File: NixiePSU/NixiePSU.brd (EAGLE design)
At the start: 55.5 x 35.5 mm, 18 parts, among them IC1 NE555, Q1 BUZ11BV, T1 BC547

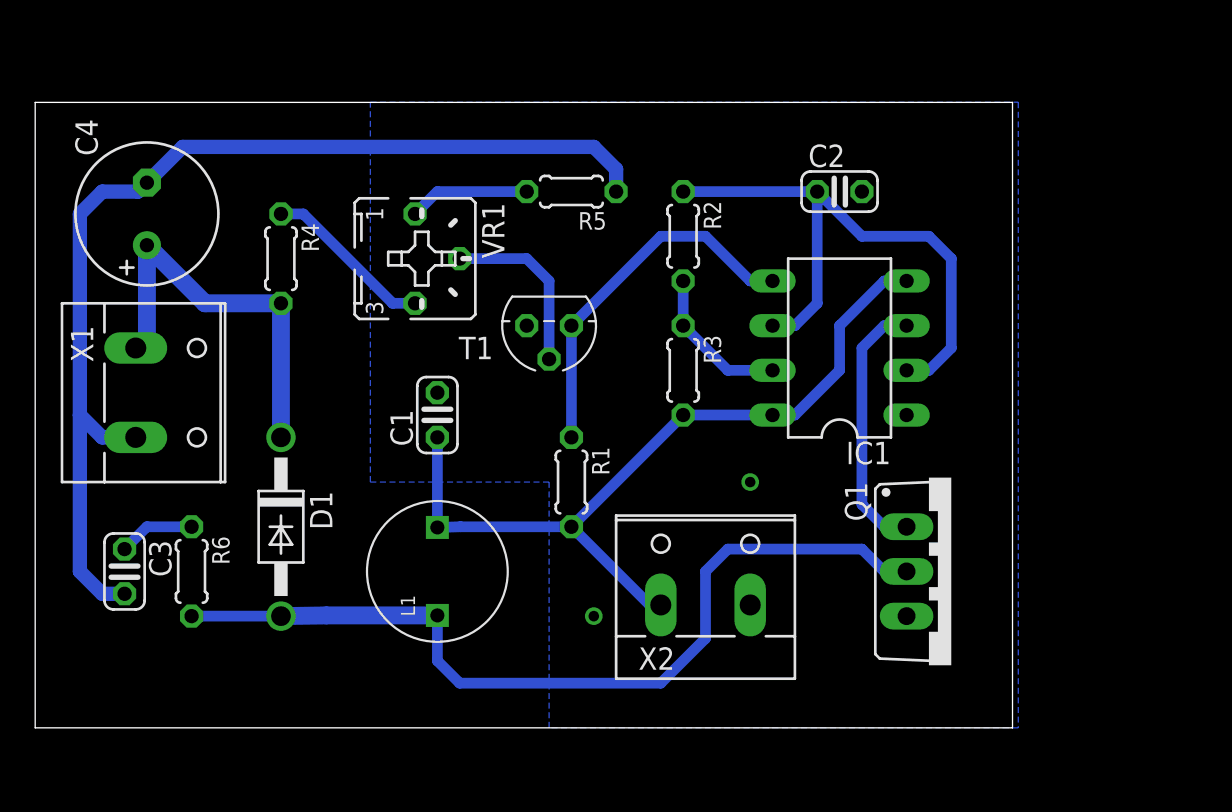
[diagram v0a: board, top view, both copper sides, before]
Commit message: Swap some components.
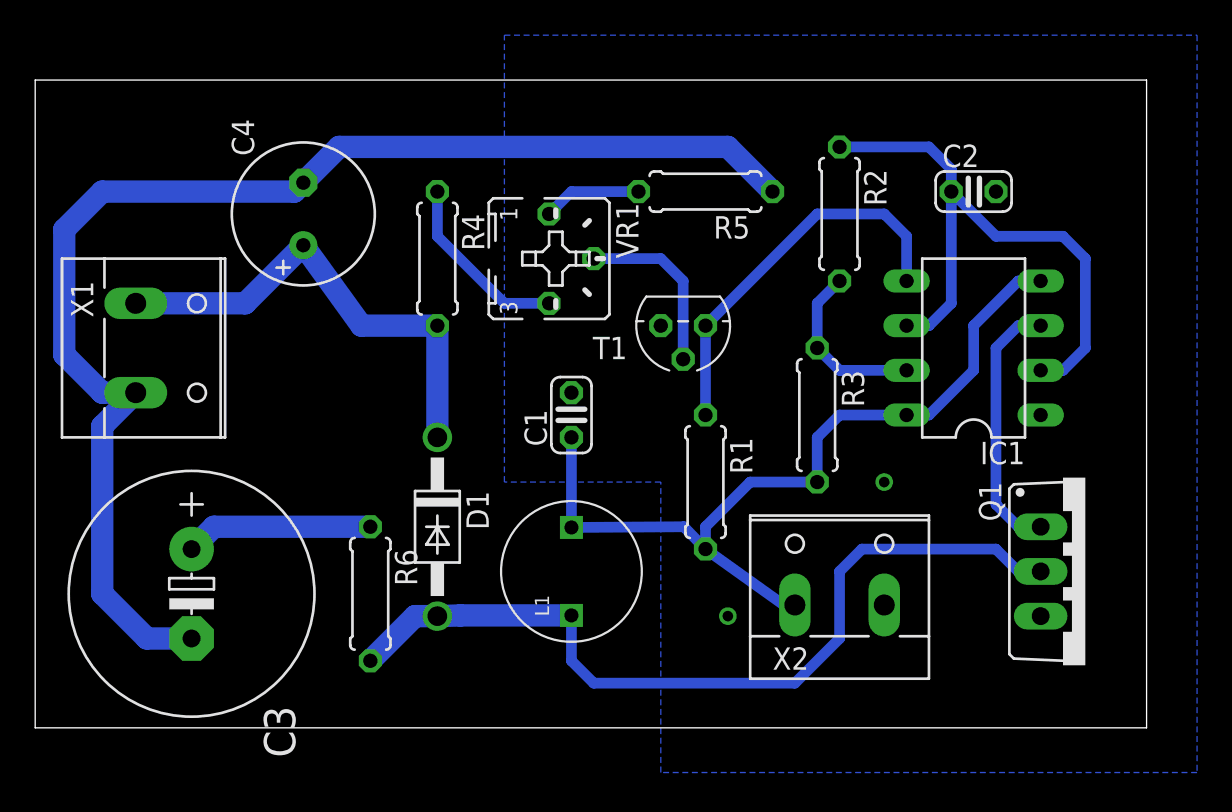
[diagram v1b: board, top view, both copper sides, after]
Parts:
- C3: device rcl:C025-024X044 -> rcl:E5-13
- R1, R2, R3, R4, R5, R6: device rcl:0204/5 -> rcl:0207/7
- moved R6 10.2 mm to (19.1, 7.62)
- moved R2 8.98 mm to (45.7, 29.2)
- moved C4 8.89 mm to (15.2, 29.2)
- moved D1 8.89 mm to (22.9, 11.4)
- moved R4 8.89 mm to (22.9, 26.7)
- moved R3 8.03 mm to (44.5, 17.8)
- moved C2 7.62 mm to (53.3, 30.5)
- moved IC1 7.62 mm to (53.3, 21.6)
- moved C1 7.62 mm to (30.5, 17.8)
- moved L1 7.62 mm to (30.5, 8.89)
- moved R1 7.62 mm to (38.1, 14.0)
- moved R5 7.62 mm to (38.1, 30.5)
- moved VR1 7.62 mm to (29.2, 26.7)
- moved Q1 7.62 mm to (59.7, 8.89)
- moved T1 7.62 mm to (36.8, 22.9)
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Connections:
- net GND: now also C3.-; no longer C3.2
- net N$9: now also C3.+; no longer C3.1
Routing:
- net GND: track 60.9 -> 73.7 mm
- net N$9: track 4.34 -> 10.7 mm
- net HV: track 22.7 -> 27.2 mm
- net VCC: track 46.0 -> 48.5 mm
- net N$2: track 49.7 -> 48.2 mm
- net N$7: track 6.88 -> 5.61 mm
- net N$5: track 20.9 -> 22.2 mm
- net N$3: track 8.67 -> 9.94 mm
- net N$4: track 9.72 -> 10.5 mm
- net N$10: track 34.4 -> 34.9 mm
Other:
- board size 55.5 x 35.5 mm -> 63.2 x 36.8 mm

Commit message: Rewire the threshold pin on the 555. Fix some ERC errors.
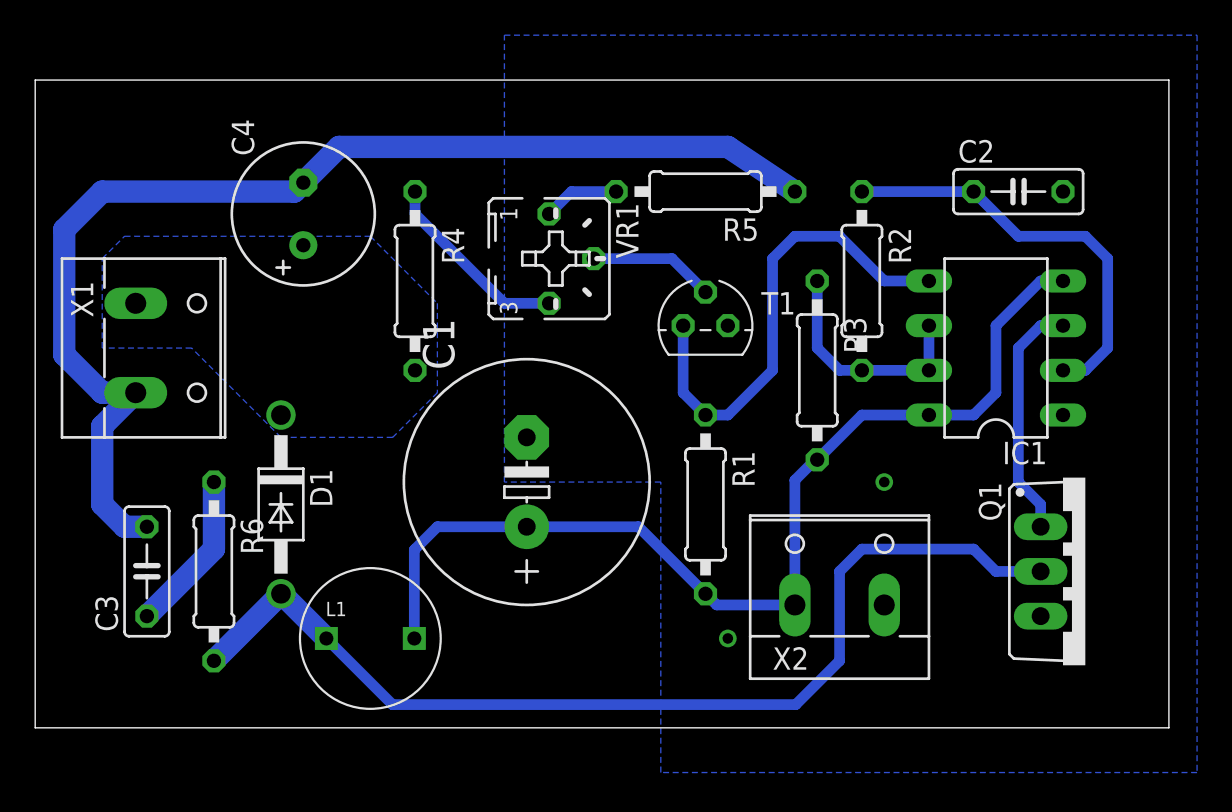
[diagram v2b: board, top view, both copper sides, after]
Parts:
- C1: device rcl:C025-024X044 -> rcl:E5-13
- C2: device rcl:C025-024X044 -> rcl:C050-025X075
- C3: device rcl:E5-13 -> rcl:C050-025X075
- R1, R2, R3, R4, R5, R6: device rcl:0207/7 -> rcl:0207/10
- moved L1 12.0 mm to (19.1, 5.08), turned to 0 degrees
- moved R6 8.98 mm to (10.2, 8.89)
- moved D1 8.98 mm to (14.0, 12.7)
- moved C1 4.58 mm to (27.9, 14.0)
- moved R2 4.02 mm to (47.0, 25.4)
- moved C3 2.84 mm to (6.35, 8.89), turned to 90 degrees
- moved C2 2.54 mm to (55.9, 30.5)
- moved R3 2.54 mm to (44.5, 20.3)
- moved R4 1.80 mm to (21.6, 25.4)
- moved T1 1.27 mm to (38.1, 22.9), turned to 0 degrees
- moved R1 1.27 mm to (38.1, 12.7)
- moved IC1 1.27 mm to (54.6, 21.6)
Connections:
- net GND: now also C1.-, C3.2; no longer C1.2, C3.-
- net N$10: no longer IC1.6
- net N$3: now also IC1.6
- net N$9: now also C3.1; no longer C3.+
- net VCC: now also C1.+; no longer C1.1
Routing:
- net HV: track 27.2 -> 0.00 mm
- net N$10: track 34.9 -> 23.7 mm
- net VCC: track 48.5 -> 59.0 mm
- net N$2: track 48.2 -> 58.3 mm
- net GND: track 73.7 -> 66.5 mm
- net N$6: track 22.2 -> 27.3 mm
- net N$3: track 9.94 -> 13.3 mm
- net N$8: track 10.1 -> 7.14 mm
- net N$9: track 10.7 -> 9.20 mm
- net N$1: track 15.0 -> 13.8 mm
- net N$7: track 5.61 -> 4.34 mm
- net N$4: track 10.5 -> 11.0 mm
- added copper zone on layer 16, net HV
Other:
- board size 63.2 x 36.8 mm -> 64.4 x 36.8 mm

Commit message: Bunch of random updated
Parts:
- R4: value 470 -> 470k
- R5: value 220k -> 1k2
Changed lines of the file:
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@@
 <?xml version="1.0" encoding="utf-8"?>
 <!DOCTYPE eagle SYSTEM "eagle.dtd">
-<eagle version="8.2.2">
+<eagle version="7.7.0">
 <drawing>
 <settings>
@@
 <grid distance="0.05" unitdist="inch" unit="inch" style="lines" multiple="1" display="no" altdistance="0.025" altunitdist="inch" altunit="inch"/>
 <layers>
-<layer number="1" name="Top" color="4" fill="1" visible="yes" active="yes"/>
-<layer number="16" name="Bottom" color="1" fill="1" visible="yes" active="yes"/>
-<layer number="17" name="Pads" color="2" fill="1" visible="yes" active="yes"/>
-<layer number="18" name="Vias" color="2" fill="1" visible="yes" active="yes"/>
-<layer number="19" name="Unrouted" color="6" fill="1" visible="yes" active="yes"/>
+<layer number="1" name="Top" color="4" fill="1" visible="no" active="yes"/>
+<layer number="16" name="Bottom" color="1" fill="1" visible="no" active="yes"/>
+<layer number="17" name="Pads" color="2" fill="1" visible="no" active="yes"/>
+<layer number="18" name="Vias" color="2" fill="1" visible="no" active="yes"/>
+<layer number="19" name="Unrouted" color="6" fill="1" visible="no" active="yes"/>
 <layer number="20" name="Dimension" color="15" fill="1" visible="yes" active="yes"/>
 <layer number="21" name="tPlace" color="7" fill="1" visible="yes" active="yes"/>
-<layer number="22" name="bPlace" color="7" fill="1" visible="yes" active="yes"/>
-<layer number="23" name="tOrigins" color="15" fill="1" visible="yes" active="yes"/>
-<layer number="24" name="bOrigins" color="15" fill="1" visible="yes" active="yes"/>
+<layer number="22" name="bPlace" color="7" fill="1" visible="no" active="yes"/>
+<layer number="23" name="tOrigins" color="15" fill="1" visible="no" active="yes"/>
+<layer number="24" name="bOrigins" color="15" fill="1" visible="no" active="yes"/>
 <layer number="25" name="tNames" color="7" fill="1" visible="yes" active="yes"/>
-<layer number="26" name="bNames" color="7" fill="1" visible="yes" active="yes"/>
+<layer number="26" name="bNames" color="7" fill="1" visible="no" active="yes"/>
 <layer number="27" name="tValues" color="7" fill="1" visible="yes" active="yes"/>
-<layer number="28" name="bValues" color="7" fill="1" visible="yes" active="yes"/>
-<layer number="29" name="tStop" color="7" fill="3" visible="yes" active="yes"/>
-<layer number="30" name="bStop" color="7" fill="6" visible="yes" active="yes"/>
-<layer number="31" name="tCream" color="7" fill="4" visible="yes" active="yes"/>
-<layer number="32" name="bCream" color="7" fill="5" visible="yes" active="yes"/>
-<layer number="33" name="tFinish" color="6" fill="3" visible="yes" active="yes"/>
-<layer number="34" name="bFinish" color="6" fill="6" visible="yes" active="yes"/>
-<layer number="35" name="tGlue" color="7" fill="4" visible="yes" active="yes"/>
-<layer number="36" name="bGlue" color="7" fill="5" visible="yes" active="yes"/>
-<layer number="37" name="tTest" color="7" fill="1" visible="yes" active="yes"/>
-<layer number="38" name="bTest" color="7" fill="1" visible="yes" active="yes"/>
-<layer number="39" name="tKeepout" color="4" fill="11" visible="yes" active="yes"/>
-<layer number="40" name="bKeepout" color="1" fill="11" visible="yes" active="yes"/>
-<layer number="41" name="tRestrict" color="4" fill="10" visible="yes" active="yes"/>
-<layer number="42" name="bRestrict" color="1" fill="10" visible="yes" active="yes"/>
-<layer number="43" name="vRestrict" color="2" fill="10" visible="yes" active="yes"/>
-<layer number="44" name="Drills" color="7" fill="1" visible="yes" active="yes"/>
-<layer number="45" name="Holes" color="7" fill="1" visible="yes" active="yes"/>
-<layer number="46" name="Milling" color="3" fill="1" visible="yes" active="yes"/>
-<layer number="47" name="Measures" color="7" fill="1" visible="yes" active="yes"/>
-<layer number="48" name="Document" color="7" fill="1" visible="yes" active="yes"/>
-<layer number="49" name="Reference" color="7" fill="1" visible="yes" active="yes"/>
-<layer number="51" name="tDocu" color="7" fill="1" visible="yes" active="yes"/>
-<layer number="52" name="bDocu" color="7" fill="1" visible="yes" active="yes"/>
+<layer number="28" name="bValues" color="7" fill="1" visible="no" active="yes"/>
+<layer number="29" name="tStop" color="7" fill="3" visible="no" active="yes"/>
+<layer number="30" name="bStop" color="7" fill="6" visible="no" active="yes"/>
+<layer number="31" name="tCream" color="7" fill="4" visible="no" active="yes"/>
+<layer number="32" name="bCream" color="7" fill="5" visible="no" active="yes"/>
+<layer number="33" name="tFinish" color="6" fill="3" visible="no" active="yes"/>
+<layer number="34" name="bFinish" color="6" fill="6" visible="no" active="yes"/>
+<layer number="35" name="tGlue" color="7" fill="4" visible="no" active="yes"/>
+<layer number="36" name="bGlue" color="7" fill="5" visible="no" active="yes"/>
+<layer number="37" name="tTest" color="7" fill="1" visible="no" active="yes"/>
+<layer number="38" name="bTest" color="7" fill="1" visible="no" active="yes"/>
+<layer number="39" name="tKeepout" color="4" fill="11" visible="no" active="yes"/>
+<layer number="40" name="bKeepout" color="1" fill="11" visible="no" active="yes"/>
+<layer number="41" name="tRestrict" color="4" fill="10" visible="no" active="yes"/>
+<layer number="42" name="bRestrict" color="1" fill="10" visible="no" active="yes"/>
+<layer number="43" name="vRestrict" color="2" fill="10" visible="no" active="yes"/>
+<layer number="44" name="Drills" color="7" fill="1" visible="no" active="yes"/>
+<layer number="45" name="Holes" color="7" fill="1" visible="no" active="yes"/>
+<layer number="46" name="Milling" color="3" fill="1" visible="no" active="yes"/>
+<layer number="47" name="Measures" color="7" fill="1" visible="no" active="yes"/>
+<layer number="48" name="Document" color="7" fill="1" visible="no" active="yes"/>
+<layer number="49" name="Reference" color="7" fill="1" visible="no" active="yes"/>
+<layer number="51" name="tDocu" color="7" fill="1" visible="no" active="yes"/>
+<layer number="52" name="bDocu" color="7" fill="1" visible="no" active="yes"/>
 <layer number="90" name="Modules" color="5" fill="1" visible="no" active="no"/>
 <layer number="91" name="Nets" color="2" fill="1" visible="no" active="no"/>
@@
 <element name="R2" library="rcl" package="0207/10" value="10k" x="46.99" y="25.4" rot="R270"/>
 <element name="R3" library="rcl" package="0207/10" value="1k" x="44.45" y="20.32" rot="R270"/>
-<element name="R4" library="rcl" package="0207/10" value="470" x="21.59" y="25.4" rot="R270"/>
-<element name="R5" library="rcl" package="0207/10" value="220k" x="38.1" y="30.48" rot="R180"/>
+<element name="R4" library="rcl" package="0207/10" value="470k" x="21.59" y="25.4" rot="R270"/>
+<element name="R5" library="rcl" package="0207/10" value="1k2" x="38.1" y="30.48" rot="R180"/>
 <element name="R6" library="rcl" package="0207/10" value="2k2" x="10.16" y="8.89" rot="R270"/>
 <element name="T1" library="transistor" package="TO92" value="BC547" x="38.1" y="22.86" smashed="yes">
